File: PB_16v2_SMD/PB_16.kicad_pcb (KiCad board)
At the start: 2 copper layers, 142.1 x 99.9 mm, 100 parts, among them J1 String1, J10 String10, J11 String11, J12 String12, J13 String13, J14 String14, J15 String15, J16 String16, J17 Power In Left, J18 Power In Right, J19 USB, J2 String2, J20 DMX1 RJ45, J21 Diff Out, J22 DMX2, J23 VIN Voltage, J24 Expansion Header, J25 RTC Conn, J26 OLED Conn, J27 GPIO Header, J28 Aux Pwr, J29 VIN Select, J3 String3, J4 String4, J5 String5, J6 String6, J7 String7, J8 String8, J9 String9, Q1 DMP3056L, SW1 DMX_LOR_Select, SW2 OLED Select, SW4 Enter BTN, SW5 Down BTN, U1 POCKETBEAGLE-SC-569, U2 OKI-78SR-5, U3 SN74HCT245N, U4 SN74HCT245N, U5 UA9638CDR, U6 TPS2051BDBVR, U7 24LC256, U8 AM26C31, U9 TPD4S009DBVR

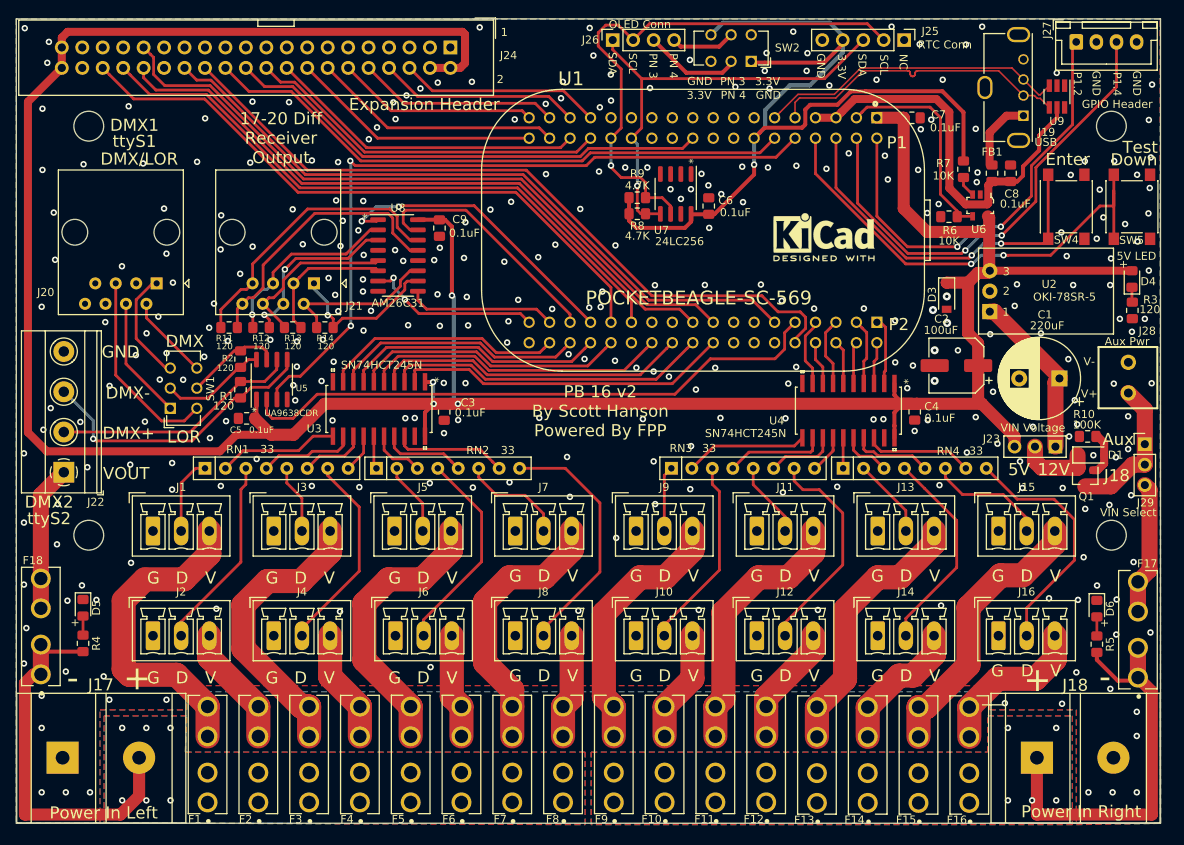
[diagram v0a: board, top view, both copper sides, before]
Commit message: Switching Array-res to Individual 33ohm
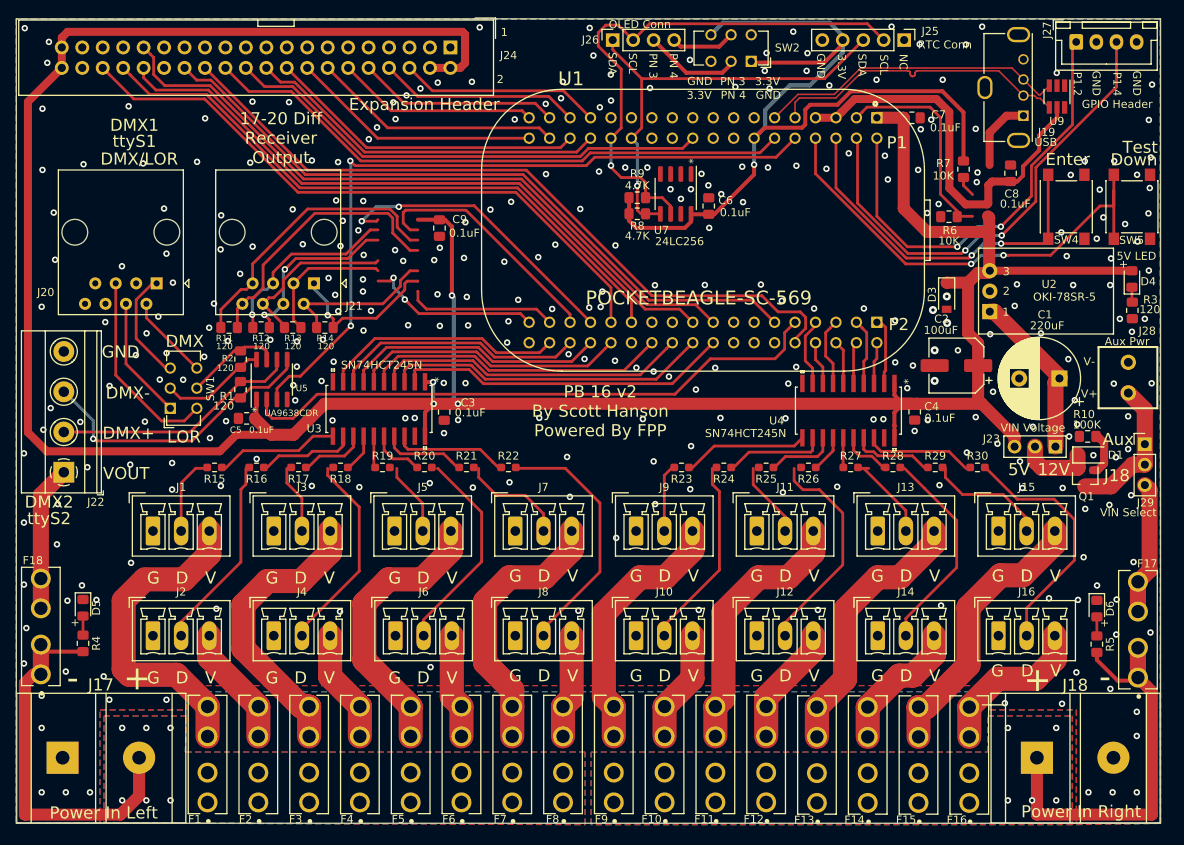
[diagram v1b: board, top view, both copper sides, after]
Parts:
- removed ?: , 
- removed FB1: 150 OHM, Inductor_SMD:L_0805_2012Metric_Pad1.15x1.40mm_HandSolder
- removed REF**: KiCad-Logo2_5mm_SilkScreen, Symbol:KiCad-Logo2_5mm_SilkScreen
- removed REF** (x4): MountingHole_3.7mm, MountingHole:MountingHole_3.7mm
- removed RN1, RN2, RN3, RN4: 33, Resistor_THT:R_Array_SIP8
- removed U6: TPS2051BDBVR, digikey-footprints:SOT-753
- removed U8: AM26C31, Package_SO:SOIC-16_3.9x9.9mm_P1.27mm
- added R15: 33, Resistor_SMD:R_0603_1608Metric_Pad0.98x0.95mm_HandSolder, F.Cu at (96.7, 108.7)
- added R16: 33, Resistor_SMD:R_0603_1608Metric_Pad0.98x0.95mm_HandSolder, F.Cu at (102.0, 108.7)
- added R17: 33, Resistor_SMD:R_0603_1608Metric_Pad0.98x0.95mm_HandSolder, F.Cu at (107.2, 108.7)
- added R18: 33, Resistor_SMD:R_0603_1608Metric_Pad0.98x0.95mm_HandSolder, F.Cu at (112.4, 108.7)
- added R19: 33, Resistor_SMD:R_0603_1608Metric_Pad0.98x0.95mm_HandSolder, F.Cu at (117.6, 108.7)
- added R20: 33, Resistor_SMD:R_0603_1608Metric_Pad0.98x0.95mm_HandSolder, F.Cu at (122.8, 108.7)
- added R21: 33, Resistor_SMD:R_0603_1608Metric_Pad0.98x0.95mm_HandSolder, F.Cu at (128.0, 108.7)
- added R22: 33, Resistor_SMD:R_0603_1608Metric_Pad0.98x0.95mm_HandSolder, F.Cu at (133.2, 108.7)
- added R23: 33, Resistor_SMD:R_0603_1608Metric_Pad0.98x0.95mm_HandSolder, F.Cu at (154.7, 108.7)
- added R24: 33, Resistor_SMD:R_0603_1608Metric_Pad0.98x0.95mm_HandSolder, F.Cu at (160.0, 108.7)
- added R25: 33, Resistor_SMD:R_0603_1608Metric_Pad0.98x0.95mm_HandSolder, F.Cu at (165.2, 108.7)
- added R26: 33, Resistor_SMD:R_0603_1608Metric_Pad0.98x0.95mm_HandSolder, F.Cu at (170.5, 108.7)
- added R27: 33, Resistor_SMD:R_0603_1608Metric_Pad0.98x0.95mm_HandSolder, F.Cu at (175.7, 108.7)
- added R28: 33, Resistor_SMD:R_0603_1608Metric_Pad0.98x0.95mm_HandSolder, F.Cu at (181.0, 108.7)
- added R29: 33, Resistor_SMD:R_0603_1608Metric_Pad0.98x0.95mm_HandSolder, F.Cu at (186.2, 108.7)
- added R30: 33, Resistor_SMD:R_0603_1608Metric_Pad0.98x0.95mm_HandSolder, F.Cu at (191.5, 108.7)
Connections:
- J10 pad 2: /Output 9-16/DOUT10 -> Net-(J10-Pad2)
- J11 pad 2: /Output 9-16/DOUT11 -> Net-(J11-Pad2)
- J14 pad 2: /Output 9-16/DOUT14 -> Net-(J14-Pad2)
- J24 pad 1: Net-(J24-Pad1) -> unconnected-(J24-Pad1)
- J24 pad 30: Net-(J24-Pad30) -> unconnected-(J24-Pad30)
- J25 pad 1: Net-(J25-Pad1) -> unconnected-(J25-Pad1)
- J9 pad 2: /Output 9-16/DOUT9 -> Net-(J9-Pad2)
- R7 pad 2: Net-(R7-Pad2) -> unconnected-(R7-Pad2)
- U9 pad 1: Net-(U9-Pad1) -> unconnected-(U9-Pad1)
- U9 pad 6: Net-(U9-Pad6) -> unconnected-(U9-Pad6)
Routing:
- net /Output 9-16/DOUT14: track 27.0 -> 0.00 mm
- net Net-(J14-Pad2): track 0.00 -> 27.0 mm
- net Net-(J10-Pad2): track 0.00 -> 24.0 mm
- net /Output 9-16/DOUT10: track 24.0 -> 0.00 mm
- net Net-(J11-Pad2): track 0.00 -> 9.42 mm
- net /Output 9-16/DOUT11: track 9.42 -> 0.00 mm
- net Net-(J9-Pad2): track 0.00 -> 8.15 mm
- net /Output 9-16/DOUT9: track 8.15 -> 0.00 mm
- net unconnected-(R7-Pad2): track 0.00 -> 2.59 mm
- net Net-(R7-Pad2): track 2.59 -> 0.00 mm
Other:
- net class 3.3v removed
- net class 5v removed
- net class Default removed
- net class Gnd removed
- net class Power removed
- net class Vin removed
- net class power2 removed
- net class usb removed
- net class v_usb removed
